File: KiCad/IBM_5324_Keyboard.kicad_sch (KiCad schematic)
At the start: 85 parts, among them SW1 CMD, SW10 ERASE, SW11 | 1, SW12 # 3, SW13 % 5, SW14 & 7, SW15 * +, SW16 ( 9, SW17 _ -, SW18 RH <-, SW19 / -, SW2 ~ `, SW20 NP 8, SW21 HOLD, SW22 FIELD ADV, SW23 W, SW24 R, SW25 Y, SW26 I, SW27 P, SW28 | \, SW29 NP 7, SW3 @ 2, SW30 NP 9, SW31 INQ, SW32 SHIFT LOCK, SW33 Q, SW34 E, SW35 T, SW36 O, SW37 ! ¢, SW38 ENTER, SW39 NP 4, SW4 $ 4, SW40 FIELD-, SW41 U, SW42 ERROR RESET, SW43 LH SHIFT, SW44 A, SW45 D, SW46 G, SW47 J, SW48 L, SW49 " ', SW5 ^ 6, SW50 } {, SW51 NP 5, SW52 NP 6, SW53 TEST, SW54 SCROLL DOWN, SW55 S, SW56 F, SW57 H, SW58 SCROLL UP, SW59 K, SW6 * 8, SW60 : ;, SW61 NEWLINE, SW62 NP 1, SW63 NP 3, SW64 ->, SW65 > <, SW66 C, SW67 B, SW68 M, SW69 . ., SW7 ) 0, SW70 RH SHIFT, SW71 NP 2, SW72 FIELD+, SW73 N, SW74 LH <-, SW75 ALT, SW76 Z, SW77 X, SW78 V, SW79 SPACE, SW8 + =, SW80 , ,, SW81 ? /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

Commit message: Update IBM_5324_Keyboard.kicad_sch
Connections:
- net Row_6: no longer SW58.2, SW64.2, SW65.2, SW66.2, SW67.2, SW68.2, SW69.2, SW70.2, SW71.2, SW72.2, SW73.2, SW74.2, SW75.2, SW76.2, SW77.2, SW78.2, SW79.2, SW80.2, SW81.2, SW82.2, SW83.2, SW84.2
- new net Row_7: SW58.2, SW64.2, SW65.2, SW66.2, SW67.2, SW68.2, SW69.2, SW70.2, SW71.2, SW72.2, SW73.2
- new net Row_8: SW74.2, SW75.2, SW76.2, SW77.2, SW78.2, SW79.2, SW80.2, SW81.2, SW82.2, SW83.2, SW84.2
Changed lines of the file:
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@@
 		)
 	)
-	(global_label "Row_6"
+	(global_label "Row_7"
 		(shape input)
 		(at 220.98 142.24 0)
@@
 		)
 	)
-	(global_label "Row_6"
+	(global_label "Row_8"
 		(shape input)
 		(at 220.98 154.94 0)

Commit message: Progressing design
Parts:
- added J1: To 5324, Clueless_Engineer:L77SDB25SA4CH4F, symbol Connector:DB25_Socket_MountingHoles
- added J2: Conn_02x14_Row_Letter_First, Connector_PinHeader_2.54mm:PinHeader_2x14_P2.54mm_Vertical, symbol Connector_Generic:Conn_02x14_Row_Letter_First
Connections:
- new net +12V: J1.12, J2.B14 (Pin_b14)
- new net DATA STROBE: J1.1, J2.B01 (Pin_b1)
- new net DELAY STROBE: J1.9, J2.B11 (Pin_b11)
- new net GND: J1.0 (PAD), J1.14 (P14), J1.15 (P15), J1.16 (P16), J1.17 (P17), J1.18 (P18), J1.19 (P19), J1.20 (P20), J1.21 (P21), J1.22 (P22), J1.23 (P23), J1.24 (P24), J1.25 (P25), J2.A01 (Pin_a1), J2.A02 (Pin_a2), J2.A03 (Pin_a3), J2.A04 (Pin_a4), J2.A05 (Pin_a5), J2.A06 (Pin_a6), J2.A07 (Pin_a7), J2.A08 (Pin_a8), J2.A09 (Pin_a9), J2.A10 (Pin_a10), J2.A11 (Pin_a11), J2.A12 (Pin_a12), J2.A13 (Pin_a13), J2.A4 (Pin_a14)
- new net PROGRAM RESET: J1.10, J2.B12 (Pin_b12)
- new net SCAN CODE BIT 0: J1.8, J2.B09 (Pin_b9)
- new net SCAN CODE BIT 1: J1.7, J2.B08 (Pin_b8)
- new net SCAN CODE BIT 2: J1.6, J2.B07 (Pin_b7)
- new net SCAN CODE BIT 3: J1.5, J2.B06 (Pin_b6)
- new net SCAN CODE BIT 4: J1.4, J2.B05 (Pin_b5)
- new net SCAN CODE BIT 5: J1.3, J2.B04 (Pin_b4)
- new net SCAN CODE BIT 6: J1.2, J2.B03 (Pin_b3)
- no-connect marks 0 -> 4

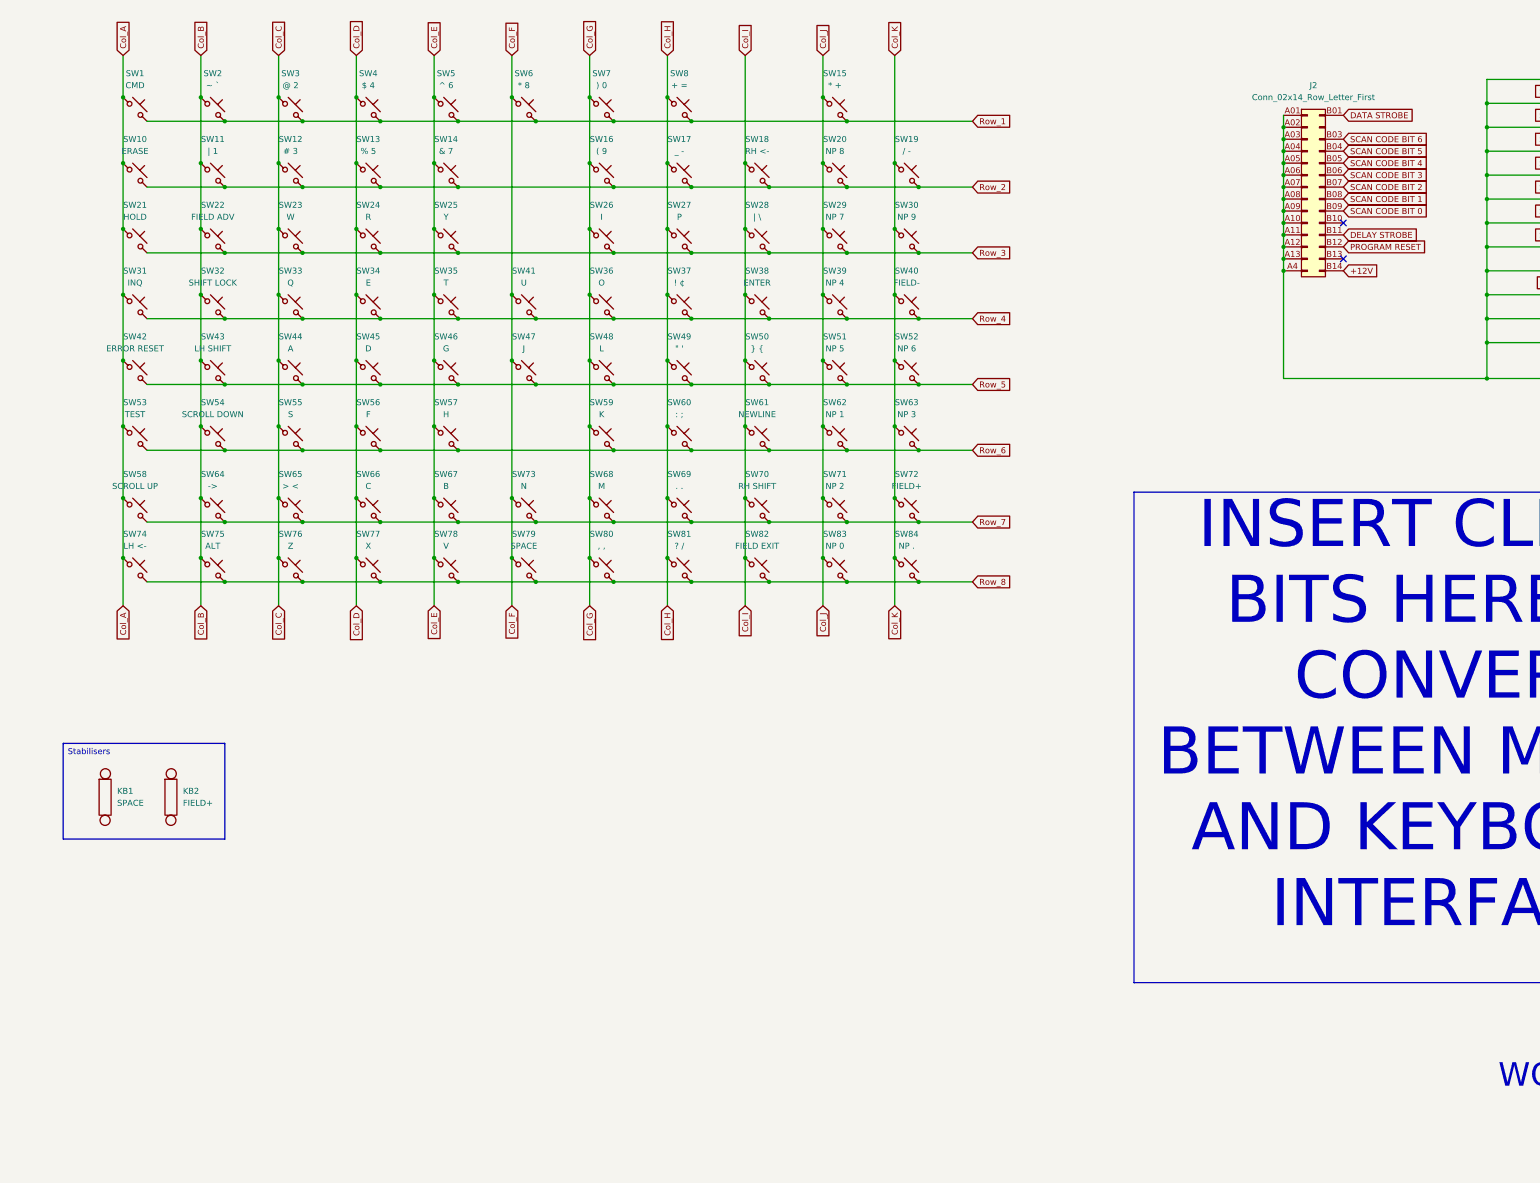
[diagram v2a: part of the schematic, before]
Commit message: Key switch routing completed
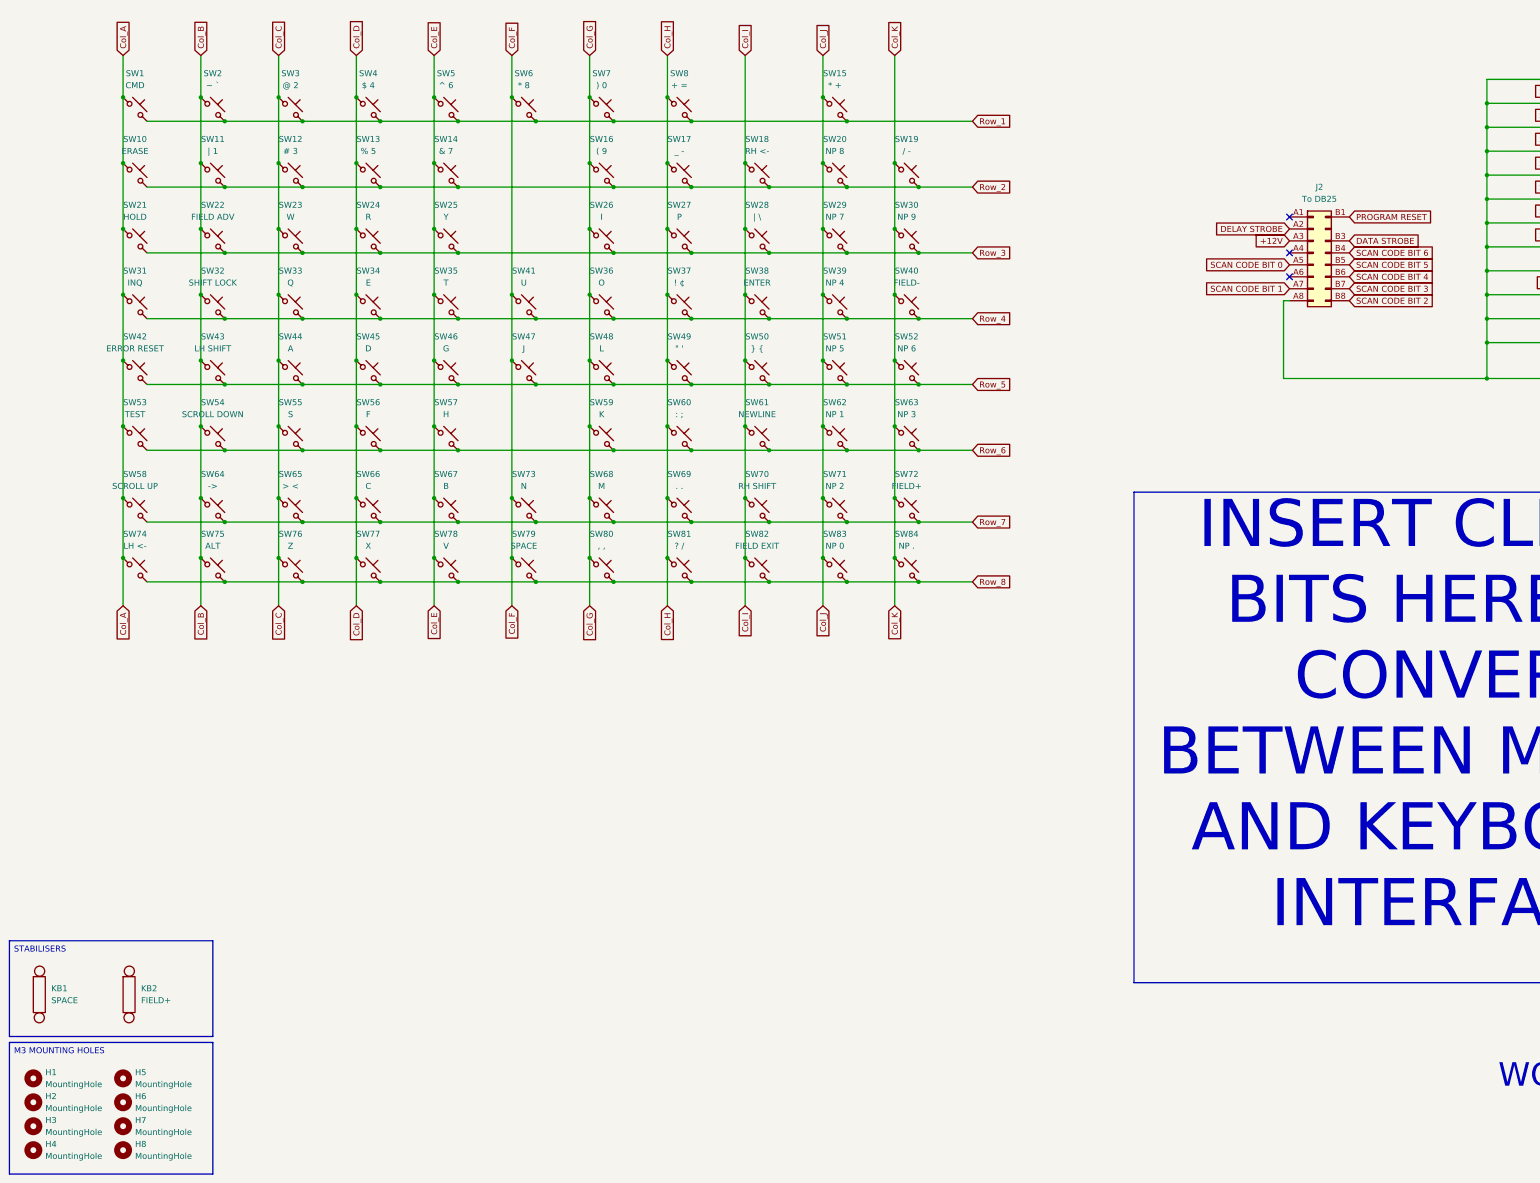
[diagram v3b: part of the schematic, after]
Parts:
- removed J2: Conn_02x14_Row_Letter_First, Connector_PinHeader_2.54mm:PinHeader_2x14_P2.54mm_Vertical, symbol Connector_Generic:Conn_02x14_Row_Letter_First
- added H1, H2, H3, H4, H5, H6, H7, H8: MountingHole, MountingHole:MountingHole_3.2mm_M3, symbol Mechanical:MountingHole
- added J2: To DB25, Connector_PinHeader_2.54mm:PinHeader_2x08_P2.54mm_Vertical, symbol Connector_Generic:Conn_02x08_Row_Letter_First
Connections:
- net +12V: now also J2.A3 (Pin_a3)
- net DATA STROBE: now also J2.B3 (Pin_b3)
- net DELAY STROBE: now also J2.A2 (Pin_a2)
- net GND: now also J2.A8 (Pin_a8)
- net PROGRAM RESET: now also J2.B1 (Pin_b1)
- net SCAN CODE BIT 0: now also J2.A5 (Pin_a5)
- net SCAN CODE BIT 1: now also J2.A7 (Pin_a7)
- net SCAN CODE BIT 2: now also J2.B8 (Pin_b8)
- net SCAN CODE BIT 3: now also J2.B7 (Pin_b7)
- net SCAN CODE BIT 4: now also J2.B6 (Pin_b6)
- net SCAN CODE BIT 5: now also J2.B5 (Pin_b5)
- net SCAN CODE BIT 6: now also J2.B4 (Pin_b4)
- no-connect marks 4 -> 5
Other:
- moved on the sheet: KB1, KB2

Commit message: Started work on firmware
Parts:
- added U1: ATmega2560-16A, Package_QFP:TQFP-100_14x14mm_P0.5mm, symbol MCU_Microchip_ATmega:ATmega2560-16A
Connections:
- new net: U1.10 (VCC), U1.31 (VCC), U1.61 (VCC), U1.80 (VCC)
- new net: U1.11 (GND), U1.32 (GND), U1.62 (GND), U1.81 (GND), U1.99 (GND)
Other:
- moved on the sheet: J1, J2, SW1, SW10, SW11, SW12, SW13, SW14, SW15, SW16, SW17, SW18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

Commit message: Started firmware development
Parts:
- removed U1: ATmega2560-16A, Package_QFP:TQFP-100_14x14mm_P0.5mm, symbol MCU_Microchip_ATmega:ATmega2560-16A
- added U1: Teensy4.1, Clueless_Engineer:Teensy41, symbol teensy:Teensy4.1
- added U2: LM7805_TO220, Package_TO_SOT_THT:TO-220-3_Horizontal_TabDown, symbol Regulator_Linear:LM7805_TO220
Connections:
- net +12V: now also U2.1 (VI)
- net GND: now also U1.1 (GND), U1.34 (GND), U1.52 (GND), U1.58 (GND), U1.59 (GND), U1.64 (GND), U2.2 (GND)
- new net +5V: U1.48 (VIN), U2.3 (VO)
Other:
- moved on the sheet: J1, J2
